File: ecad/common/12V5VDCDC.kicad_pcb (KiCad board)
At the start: 2 copper layers, 11 parts, among them U4 MIC4680YM

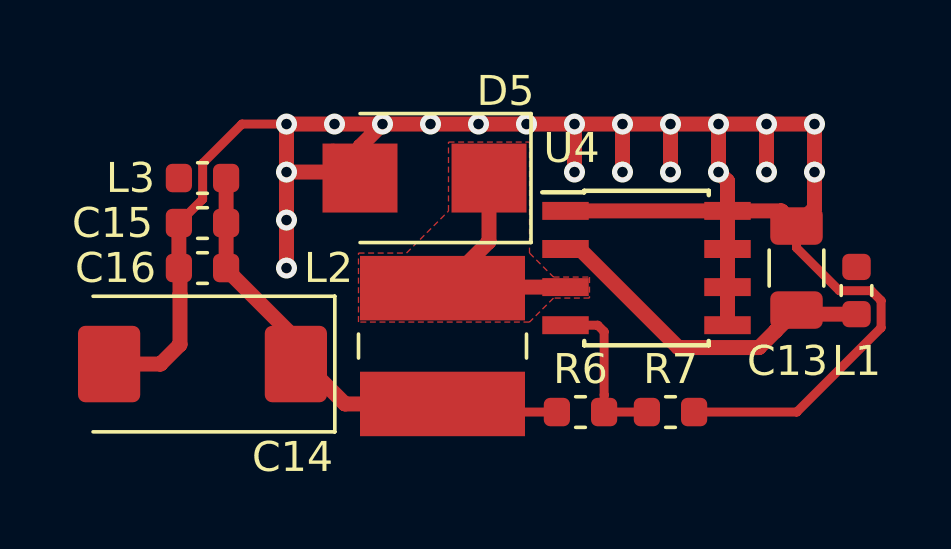
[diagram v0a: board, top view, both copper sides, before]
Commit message: Adds TVS diode on fan connector
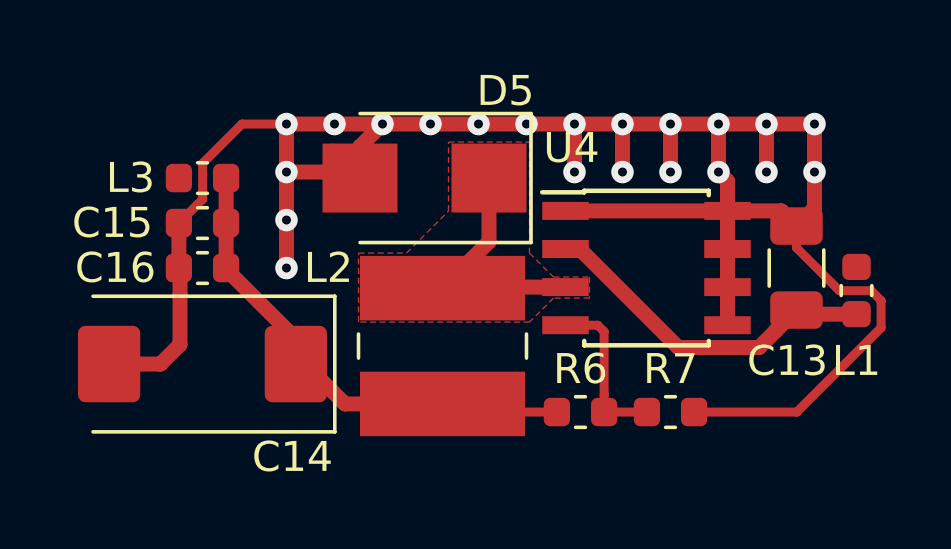
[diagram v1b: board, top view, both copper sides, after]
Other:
- net class Default: via_dia 0.7 -> 0.75; via_drill 0.35 -> 0.3
- net class Power: via_dia 0.7 -> 0.75; via_drill 0.35 -> 0.3
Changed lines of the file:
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@@
     (segment_width 0.2)
     (edge_width 0.1)
-    (via_size 0.7)
-    (via_drill 0.35)
+    (via_size 0.75)
+    (via_drill 0.3)
     (via_min_size 0.4)
     (via_min_drill 0.3)
@@
     (clearance 0.195)
     (trace_width 0.3)
-    (via_dia 0.7)
-    (via_drill 0.35)
+    (via_dia 0.75)
+    (via_drill 0.3)
     (uvia_dia 0.3)
     (uvia_drill 0.1)
@@
     (clearance 0.195)
     (trace_width 0.5)
-    (via_dia 0.7)
-    (via_drill 0.35)
+    (via_dia 0.75)
+    (via_drill 0.3)
     (uvia_dia 0.3)
     (uvia_drill 0.1)
@@
   (segment (start 150.7 101.905) (end 150.7 100.635) (width 0.5) (layer F.Cu) (net 2))
   (segment (start 136 95.2) (end 137.6 95.2) (width 0.5) (layer F.Cu) (net 2))
-  (via (at 136 96.8) (size 0.7) (drill 0.35) (layers F.Cu B.Cu) (net 2))
-  (via (at 136 98.4) (size 0.7) (drill 0.35) (layers F.Cu B.Cu) (net 2))
-  (via (at 136 100) (size 0.7) (drill 0.35) (layers F.Cu B.Cu) (net 2))
-  (via (at 137.6 95.2) (size 0.7) (drill 0.35) (layers F.Cu B.Cu) (net 2))
-  (via (at 139.2 95.2) (size 0.7) (drill 0.35) (layers F.Cu B.Cu) (net 2))
-  (via (at 140.8 95.2) (size 0.7) (drill 0.35) (layers F.Cu B.Cu) (net 2))
-  (via (at 142.4 95.2) (size 0.7) (drill 0.35) (layers F.Cu B.Cu) (net 2))
-  (via (at 144 95.2) (size 0.7) (drill 0.35) (layers F.Cu B.Cu) (net 2))
-  (via (at 145.6 95.2) (size 0.7) (drill 0.35) (layers F.Cu B.Cu) (net 2))
-  (via (at 147.2 95.2) (size 0.7) (drill 0.35) (layers F.Cu B.Cu) (net 2))
-  (via (at 148.8 95.2) (size 0.7) (drill 0.35) (layers F.Cu B.Cu) (net 2))
-  (via (at 150.4 95.2) (size 0.7) (drill 0.35) (layers F.Cu B.Cu) (net 2))
-  (via (at 152 95.2) (size 0.7) (drill 0.35) (layers F.Cu B.Cu) (net 2))
-  (via (at 153.6 95.2) (size 0.7) (drill 0.35) (layers F.Cu B.Cu) (net 2))
-  (via (at 145.6 96.8) (size 0.7) (drill 0.35) (layers F.Cu B.Cu) (net 2))
-  (via (at 147.2 96.8) (size 0.7) (drill 0.35) (layers F.Cu B.Cu) (net 2))
-  (via (at 148.8 96.8) (size 0.7) (drill 0.35) (layers F.Cu B.Cu) (net 2))
-  (via (at 150.4 96.8) (size 0.7) (drill 0.35) (layers F.Cu B.Cu) (net 2))
-  (via (at 152 96.8) (size 0.7) (drill 0.35) (layers F.Cu B.Cu) (net 2))
-  (via (at 153.6 96.8) (size 0.7) (drill 0.35) (layers F.Cu B.Cu) (net 2))
+  (via (at 136 96.8) (size 0.75) (drill 0.3) (layers F.Cu B.Cu) (net 2))
+  (via (at 136 98.4) (size 0.75) (drill 0.3) (layers F.Cu B.Cu) (net 2))
+  (via (at 136 100) (size 0.75) (drill 0.3) (layers F.Cu B.Cu) (net 2))
+  (via (at 137.6 95.2) (size 0.75) (drill 0.3) (layers F.Cu B.Cu) (net 2))
+  (via (at 139.2 95.2) (size 0.75) (drill 0.3) (layers F.Cu B.Cu) (net 2))
+  (via (at 140.8 95.2) (size 0.75) (drill 0.3) (layers F.Cu B.Cu) (net 2))
+  (via (at 142.4 95.2) (size 0.75) (drill 0.3) (layers F.Cu B.Cu) (net 2))
+  (via (at 144 95.2) (size 0.75) (drill 0.3) (layers F.Cu B.Cu) (net 2))
+  (via (at 145.6 95.2) (size 0.75) (drill 0.3) (layers F.Cu B.Cu) (net 2))
+  (via (at 147.2 95.2) (size 0.75) (drill 0.3) (layers F.Cu B.Cu) (net 2))
+  (via (at 148.8 95.2) (size 0.75) (drill 0.3) (layers F.Cu B.Cu) (net 2))
+  (via (at 150.4 95.2) (size 0.75) (drill 0.3) (layers F.Cu B.Cu) (net 2))
+  (via (at 152 95.2) (size 0.75) (drill 0.3) (layers F.Cu B.Cu) (net 2))
+  (via (at 153.6 95.2) (size 0.75) (drill 0.3) (layers F.Cu B.Cu) (net 2))
+  (via (at 145.6 96.8) (size 0.75) (drill 0.3) (layers F.Cu B.Cu) (net 2))
+  (via (at 147.2 96.8) (size 0.75) (drill 0.3) (layers F.Cu B.Cu) (net 2))
+  (via (at 148.8 96.8) (size 0.75) (drill 0.3) (layers F.Cu B.Cu) (net 2))
+  (via (at 150.4 96.8) (size 0.75) (drill 0.3) (layers F.Cu B.Cu) (net 2))
+  (via (at 152 96.8) (size 0.75) (drill 0.3) (layers F.Cu B.Cu) (net 2))
+  (via (at 153.6 96.8) (size 0.75) (drill 0.3) (layers F.Cu B.Cu) (net 2))
   (segment (start 152.495 98.095) (end 153 98.6) (width 0.5) (layer F.Cu) (net 2))
   (segment (start 150.7 98.095) (end 152.495 98.095) (width 0.5) (layer F.Cu) (net 2))
@@
   (segment (start 132.4125 98.5) (end 133.20499 97.70751) (width 0.3) (layer F.Cu) (net 2))
   (segment (start 136 95.2) (end 136 95.2) (width 0.5) (layer F.Cu) (net 2))
-  (via (at 136 95.2) (size 0.7) (drill 0.35) (layers F.Cu B.Cu) (net 2))
+  (via (at 136 95.2) (size 0.75) (drill 0.3) (layers F.Cu B.Cu) (net 2))
   (segment (start 136.375 103.2) (end 136.375 102.425) (width 0.5) (layer F.Cu) (net 3))
   (segment (start 136.375 102.425) (end 133.95 100) (width 0.5) (layer F.Cu) (net 3))
